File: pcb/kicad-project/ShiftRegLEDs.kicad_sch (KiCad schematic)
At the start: 18 parts, among them U5 74HC595

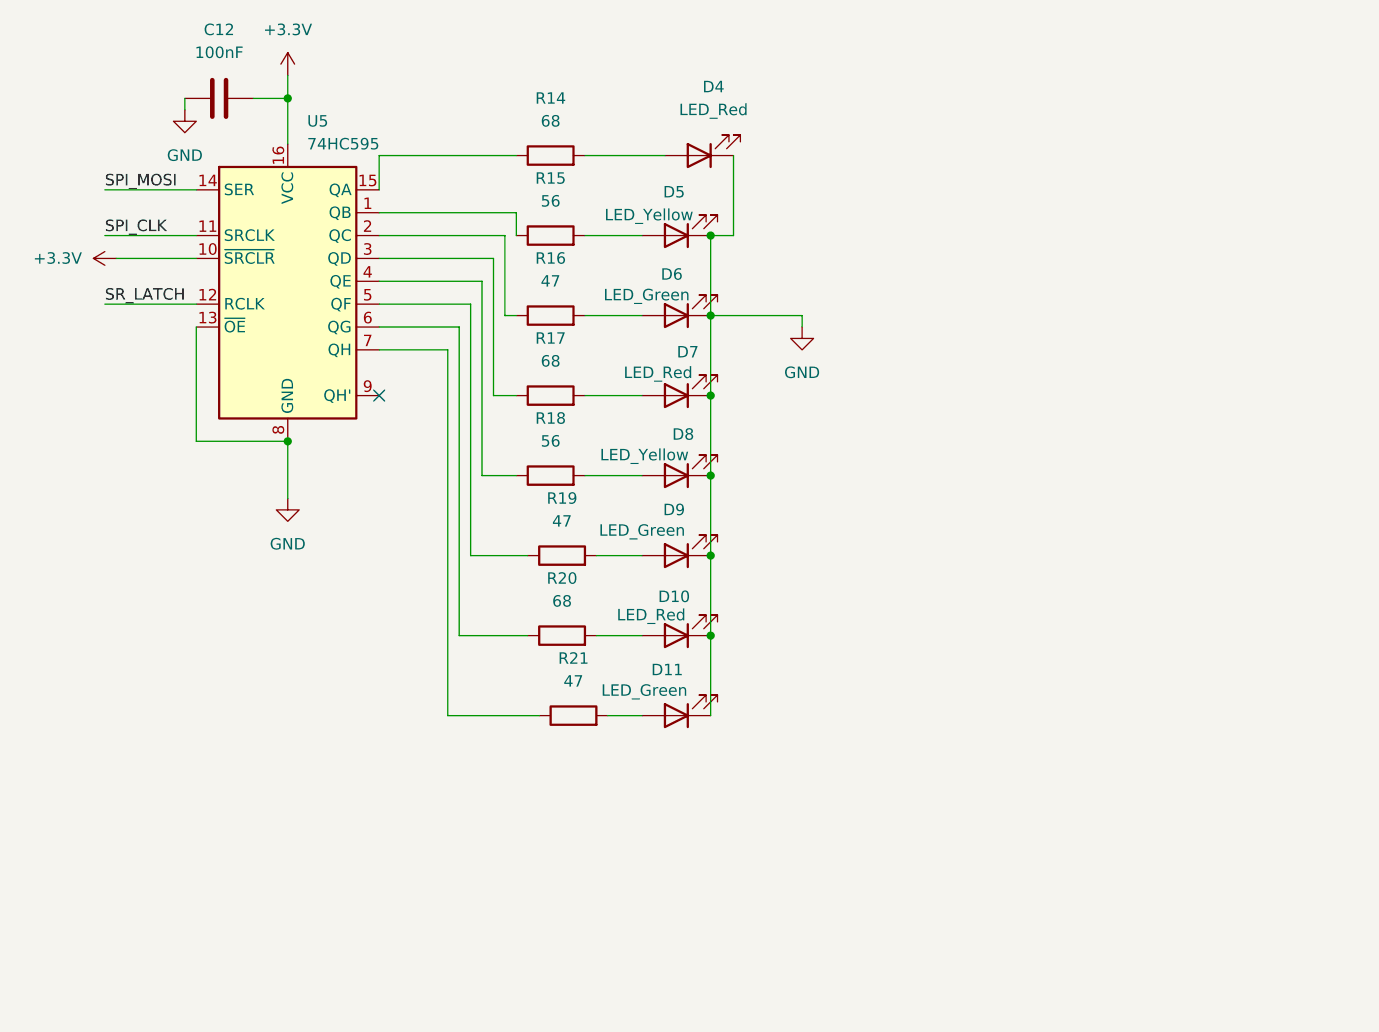
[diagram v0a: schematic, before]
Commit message: Added appropriate footprints to all components in the PCB
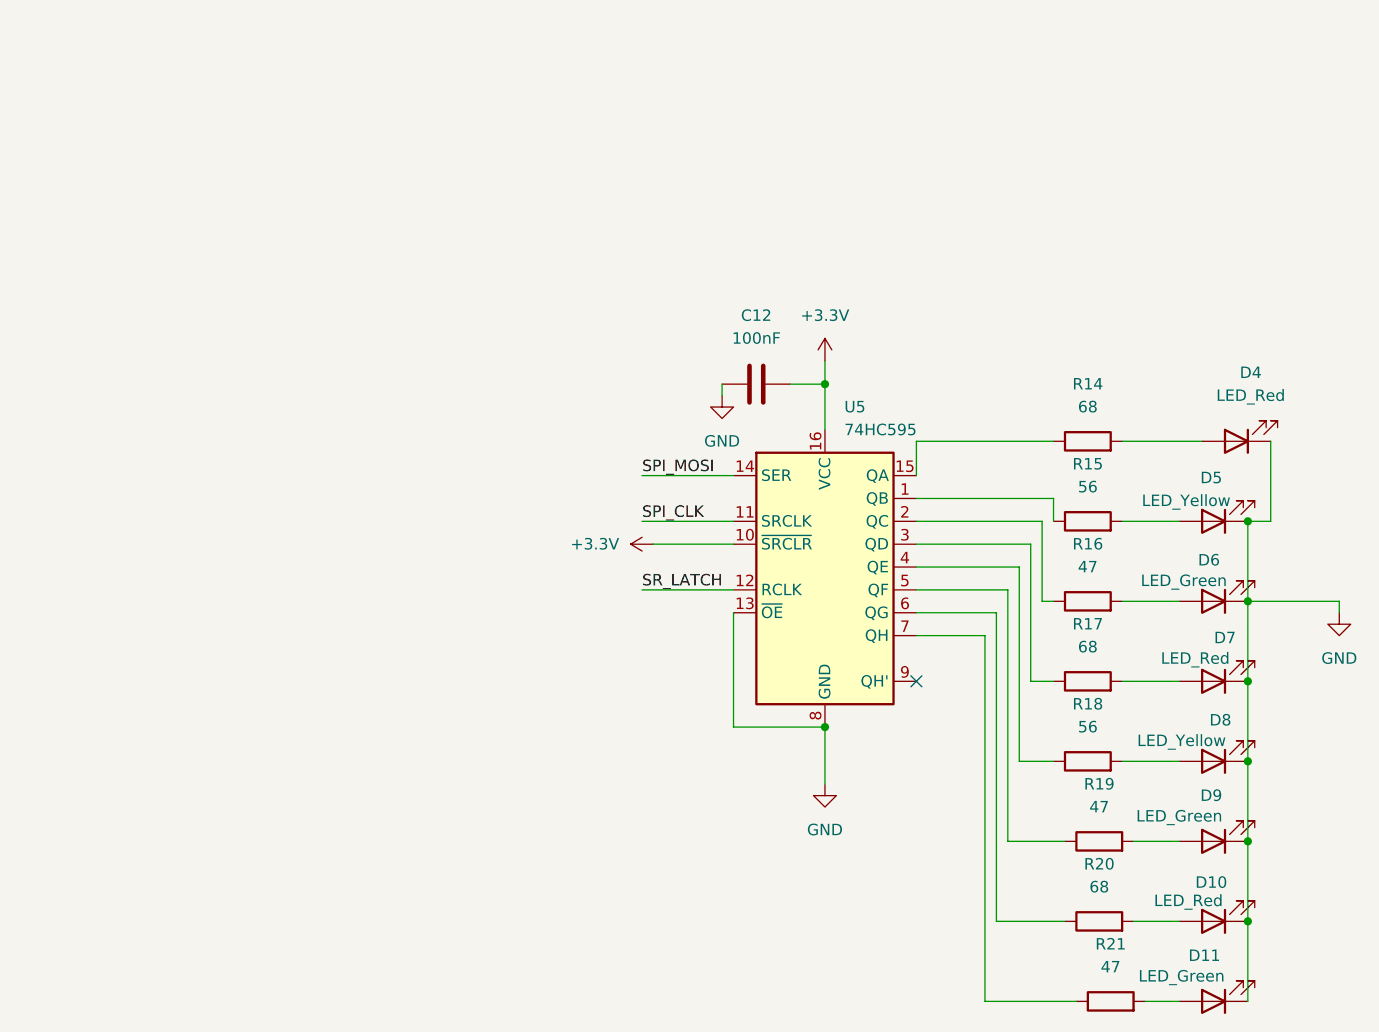
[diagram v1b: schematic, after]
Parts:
- C12: footprint (none) -> Capacitor_SMD:C_0805_2012Metric
- D10, D11, D4, D5, D6, D7, D8, D9: footprint (none) -> LED_THT:LED_D5.0mm
- R14, R15, R16, R17, R18, R19, R20, R21: footprint (none) -> Resistor_SMD:R_0805_2012Metric
- U5: footprint (none) -> Package_DIP:DIP-16_W7.62mm
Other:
- moved on the sheet: C12, D10, D11, D4, D5, D6, D7, D8, D9, R14, R15, R16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
